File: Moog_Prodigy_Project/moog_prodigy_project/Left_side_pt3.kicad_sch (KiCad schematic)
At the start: 52 parts, among them J1 P2-3, J2 P2-4, J3 P2-2, J4 P2-1, J5 P2-1, SW6 Switch_4x4, SW7 SW_Slide_DPDT_3x3, SW9 Switch_1x3, U12B1 OPA134, U13 NE5532, U14 AD8001AR, U2 NE5532, U2B2 OPA134, U67 OPA134

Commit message: PCB priprema i fix gresaka
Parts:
- removed J1: P2-3, Connector:Banana_Cliff_FCR7350B_S16N-PC_Horizontal, symbol CT3151-2:CT3151-2
- removed J2: P2-4, Connector:Banana_Cliff_FCR7350B_S16N-PC_Horizontal, symbol CT3151-2:CT3151-2
- removed J3: P2-2, Connector:Banana_Cliff_FCR7350B_S16N-PC_Horizontal, symbol CT3151-2:CT3151-2
- removed J4, J5: P2-1, Connector:Banana_Cliff_FCR7350B_S16N-PC_Horizontal, symbol CT3151-2:CT3151-2
- removed SW9: Switch_1x3, symbol Switch:DPDT2
- removed U14: AD8001AR, Package_SO:SOIC-8_3.9x4.9mm_P1.27mm, symbol Amplifier_Operational:AD8001AR
- removed U2B2: OPA134, OPA134PA:DIP794W45P254L959H508Q8, symbol Amplifier_Operational:OPA134
- added J1: P2-3, Connector:Banana_Cliff_FCR7350B_S16N-PC_Horizontal, symbol Connector_Generic:Conn_01x01
- added J2: P2-4, Connector:Banana_Cliff_FCR7350B_S16N-PC_Horizontal, symbol Connector_Generic:Conn_01x01
- added J3: P2-2, Connector:Banana_Cliff_FCR7350B_S16N-PC_Horizontal, symbol Connector_Generic:Conn_01x01
- added J4, J5: P2-1, Connector:Banana_Cliff_FCR7350B_S16N-PC_Horizontal, symbol Connector_Generic:Conn_01x01
- added SW9: Switch_1x3, ATE1D-2M3-10-Z_1x2:SW_ATE1D-2M3-10-Z, symbol Switch:SW_SPDT
- added unit 1 of U12
- added U3: NE5532, NE5532AP:DIP794W45P254L1016H508Q8, symbol Amplifier_Operational:NE5532
- added U4: OPA134, OPA134PA:DIP794W45P254L959H508Q8, symbol Comparator:MCP6562
- added unit 1 of UI1
- added unit 3 of UI1
- R29, R79: footprint Resistor_THT:R_Axial_DIN0207_L6.3mm_D2.5mm_P7.62mm_Horizontal -> Potentiometer_THT:Potentiometer_ACP_CA9-V10_Vertical
- R92, R98: footprint Resistor_THT:R_Axial_DIN0207_L6.3mm_D2.5mm_P7.62mm_Horizontal -> Potentiometer_THT:Potentiometer_Runtron_RM-065_Vertical
- RV88: renamed from R88; footprint Resistor_THT:R_Axial_DIN0207_L6.3mm_D2.5mm_P7.62mm_Horizontal -> Potentiometer_THT:Potentiometer_ACP_CA9-V10_Vertical
- renumbered U12B1 to U12
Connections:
- net +12V: now also J5.1 (Pin_1), U3.8 (V+), U4.8 (V+), UI1.8 (V+)
- net -12V: now also U3.4 (V-), U4.4 (V-), UI1.4 (V-)
- net at C23.1, R82.2: now also U12.7; no longer U12.1
- net at C23.2, R85.2: now also U12.6 (-); no longer U12.2 (-)
- net at R81.1: now also U12.5 (+), J3.1 (Pin_1); no longer U12.3 (+)
- net at R86.2, R87.1, R89.2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: now also UI1.2 (-)
- net at C21.2, UI4.4: now also U12.3 (+)
- net at C22.2, R83.1, UI1.5 (+): now also J1.1 (Pin_1)
- net at R170.1: now also J4.1 (Pin_1)
- net at R104.1, R105.2: now also SW9.3 (C)
- net at R90.2, R91.1: now also UI1.3 (+)
- net at R85.1, R95.1, SW6.6 (F): now also U12.1, U12.2 (-)
- net at C24.1, R98.2, U13.2 (-): now also SW9.1 (A)
- net at U13.5 (+): now also SW9.2 (B)
- net at C22.1, UI1.7: now also J2.1 (Pin_1)
- net at R87.2: now also UI1.1
- no-connect marks 13 -> 11
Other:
- moved on the sheet: CR1, CR2, R105, R29, R83, R84, R86, R89, RV88, U13B, UI1B

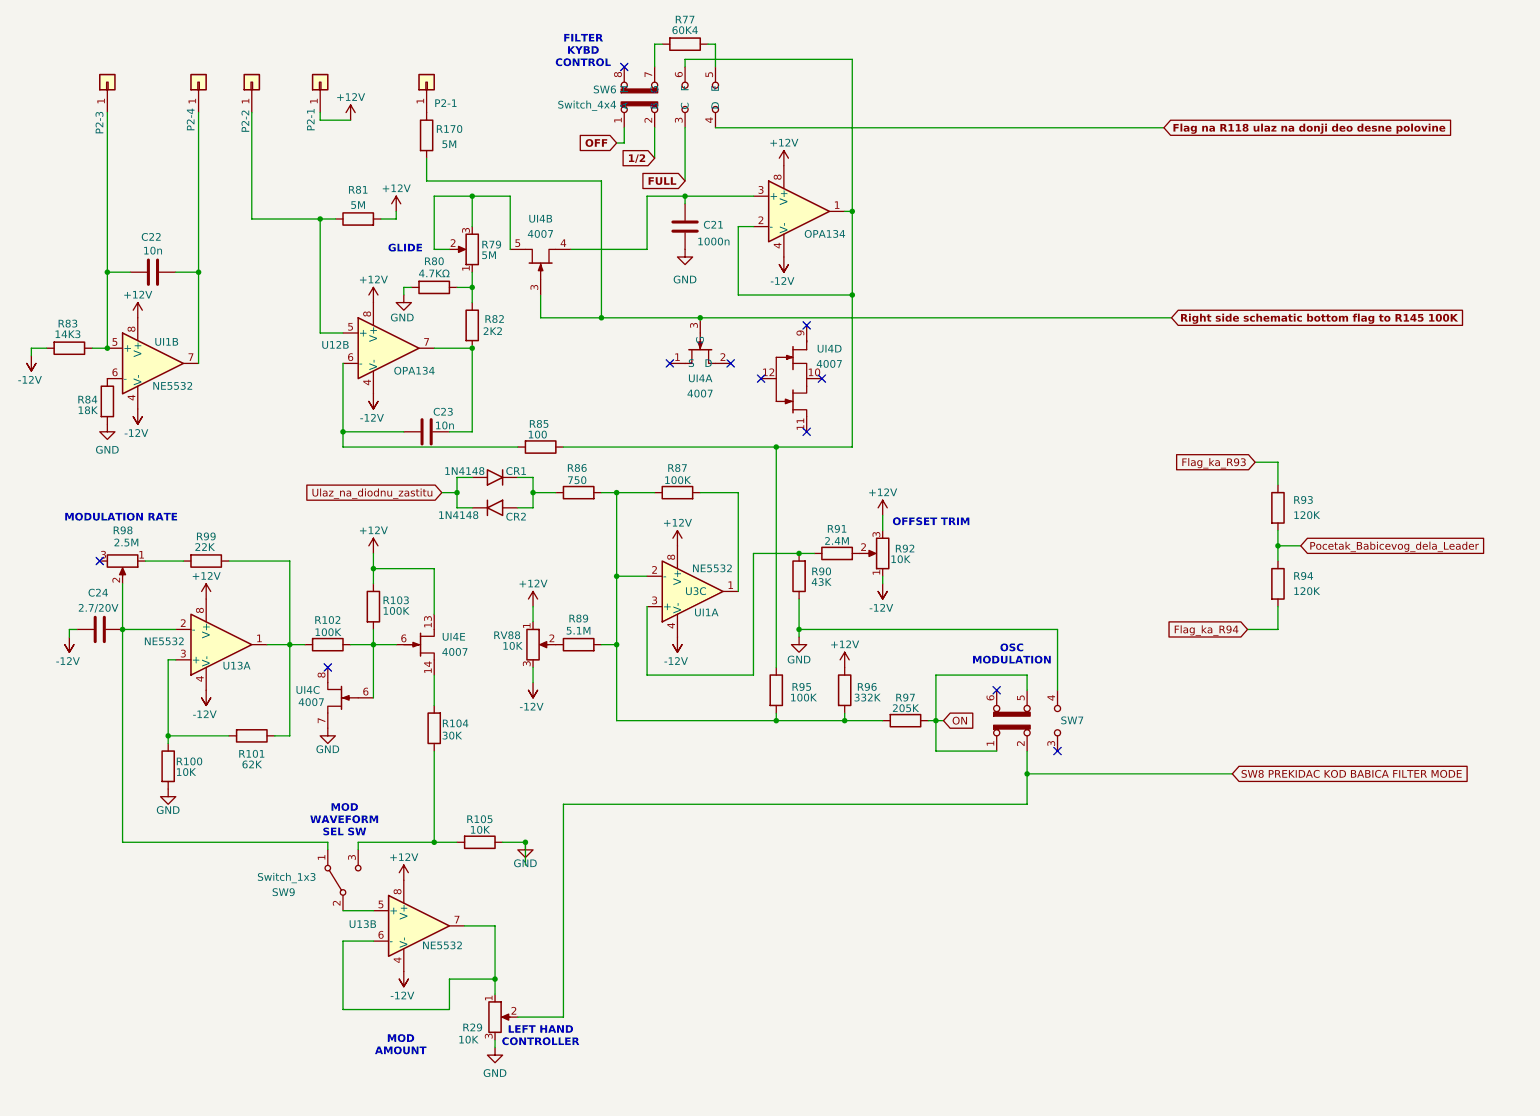
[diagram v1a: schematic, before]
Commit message: problemi sa ca3096, multiplicirani footprintovi
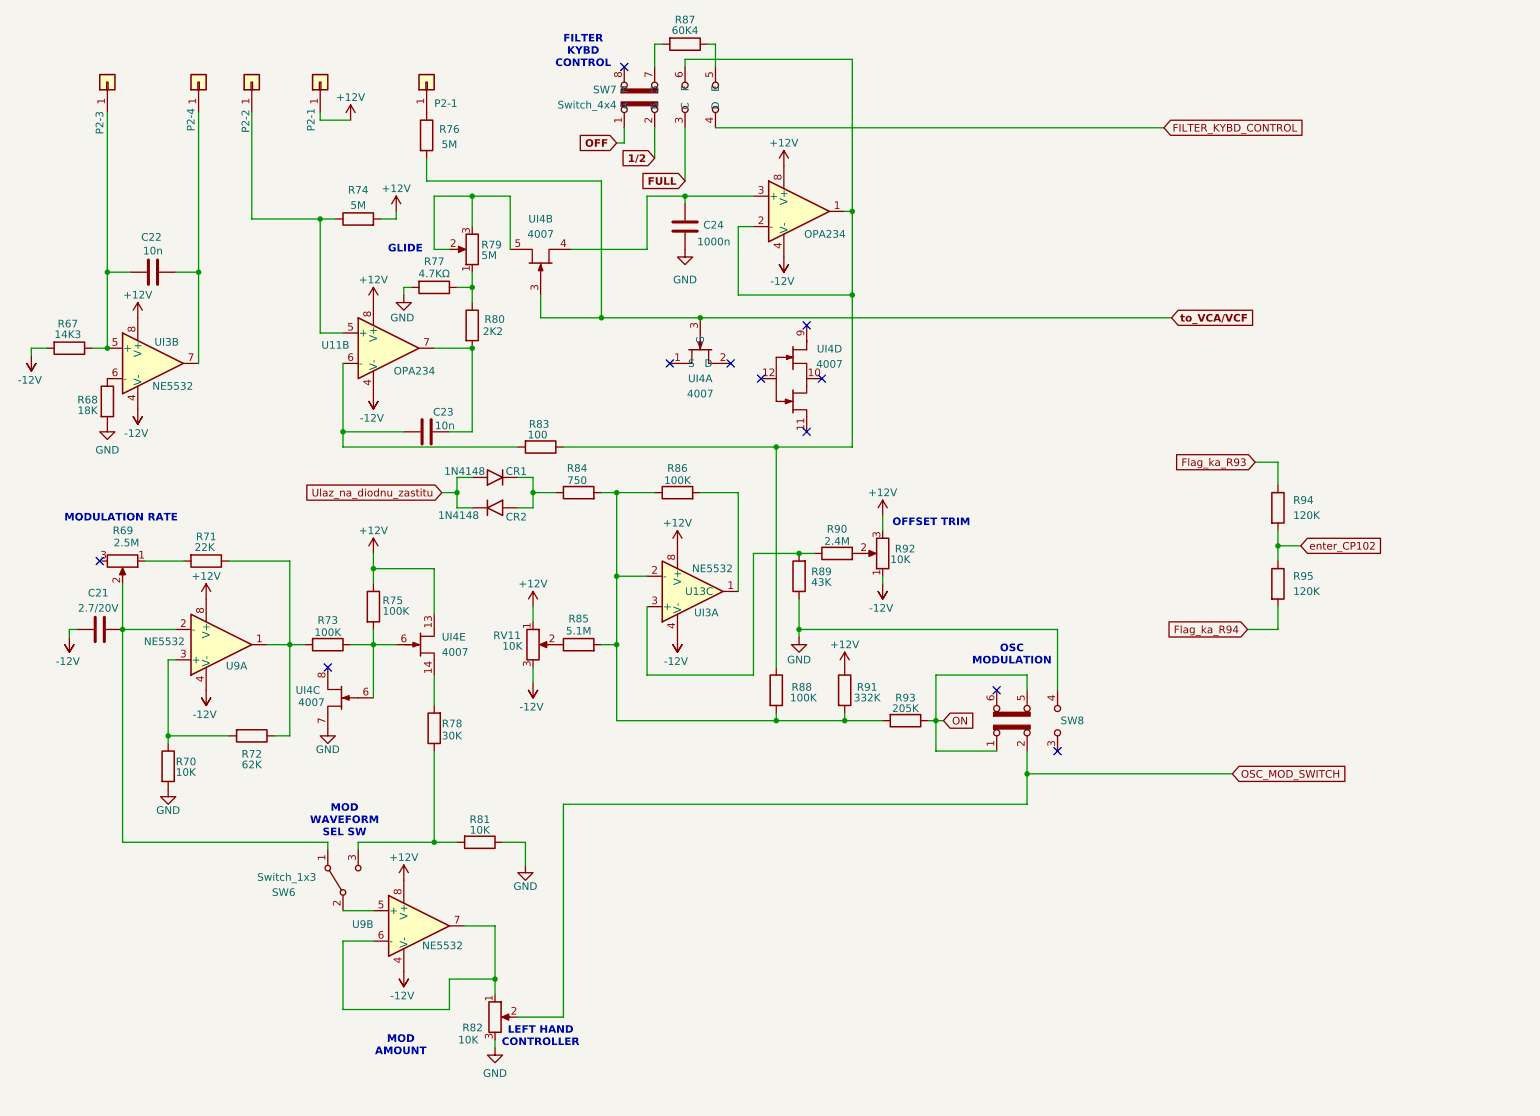
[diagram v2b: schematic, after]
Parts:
- SW8: renamed from SW7; footprint CL-SB-22A-02T_3x3:SW_CL-SB-22A-02T -> Button_Switch_THT:SW_CK_JS202011CQN_DPDT_Straight
- U11: renamed from U12; value OPA134 -> OPA234
- UI4: footprint MC14007UBDG:SOIC127P600X175-14N -> Package_DIP:DIP-14_W7.62mm_Socket
- renumbered C24 to C21, C21 to C24, J5 to J4, J4 to J5, R83 to R67, R84 to R68, R98 to R69, R100 to R70, R99 to R71, R101 to R72, R102 to R73, R81 to R74, R103 to R75, R170 to R76, R80 to R77, R104 to R78, R82 to R80, R105 to R81, R29 to R82, R85 to R83, R86 to R84, R89 to R85, R87 to R86, R77 to R87, R95 to R88, R90 to R89, R91 to R90, R96 to R91, R97 to R93, R93 to R94, R94 to R95, RV88 to RV11, SW9 to SW6, SW6 to SW7, U2 to U10, U67 to U12, U3 to U13, U4 to U14, U13 to U9, UI1 to UI3
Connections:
- net Flag na  R118 ulaz na donji deo desne polovine renamed FILTER_KYBD_CONTROL
- net Pocetak_Babicevog_dela_Leader renamed enter_CP102
- net Right side schematic bottom flag to R145 100K renamed to_VCA/VCF
- net SW8 PREKIDAC KOD BABICA FILTER MODE renamed OSC_MOD_SWITCH

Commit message: Fix 1 nakon review-a 27.05.2026
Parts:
- removed R92: 10K, Potentiometer_THT:Potentiometer_Runtron_RM-065_Vertical, symbol Device:R_Potentiometer
- added RV92: 10K, Potentiometer_THT:Potentiometer_Bourns_3339P_Vertical_HandSoldering, symbol Device:R_Potentiometer_Trim
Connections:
- net +12V: now also UI4., RV92.3; no longer UI4.13
- net -12V: now also RV92.1
- net GND: now also UI4.; no longer UI4.7
- net to_VCA/VCF: now also UI4., UI4.; no longer UI4.3, UI4.3 (G)
- net at R73.1, R75.2: now also UI4., UI4.; no longer UI4.6, UI4.6
- net at C24.2, U11.3 (+): now also UI4.; no longer UI4.4
- net at R78.2: now also UI4.; no longer UI4.14
- net at R90.2: now also RV92.2
- net at R79.2, R79.3: now also UI4.; no longer UI4.5
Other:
- title: (none) -> Treći segment leve strane šeme

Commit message: Latest checkpoints update 05.06.2026
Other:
- note added: "Oblik signala po položaju preklopnika Trouga - levi položaj Četvrtka - desni položaj"
- note added: "Paljenje OSC modulacije: ON - levi položaj preklopnika OFF - desni položaj preklopnika"
- moved on the sheet: C23, R83, SW6
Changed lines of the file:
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@@
 		(comment 4 "Jovan Mastelica E1 105/2023")
 	)
+	(text "Oblik signala po položaju preklopnika\nTrouga - levi položaj\nČetvrtka - desni položaj"
+		(exclude_from_sim no)
+		(at 48.768 147.066 0)
+		(effects
+			(font
+				(size 1.27 1.27)
+			)
+			(justify left)
+		)
+	)
 	(text "OFFSET TRIM"
 		(exclude_from_sim no)
@@
 	(text "OSC\nMODULATION"
 		(exclude_from_sim no)
-		(at 182.88 119.888 0)
+		(at 178.308 139.446 0)
 		(effects
 			(font
@@
 	(text "MOD \nWAVEFORM \nSEL SW"
 		(exclude_from_sim no)
-		(at 71.374 147.574 0)
+		(at 55.372 155.702 0)
 		(effects
 			(font
@@
 		)
 	)
+	(text "Paljenje OSC modulacije:\nON - levi položaj preklopnika\nOFF - desni položaj preklopnika"
+		(exclude_from_sim no)
+		(at 169.418 118.872 0)
+		(effects
+			(font
+				(size 1.27 1.27)
+			)
+			(justify left)
+		)
+	)
 	(text "MODULATION RATE"
 		(exclude_from_sim no)
@@
 	)
 	(junction
+		(at 71.12 82.55)
+		(diameter 0)
+		(color 0 0 0 0)
+	)
+	(junction
 		(at 90.17 92.71)
 		(diameter 0)
@@
 	)
 	(junction
-		(at 71.12 82.55)
-		(diameter 0)
-		(color 0 0 0 0)
-	)
-	(junction
 		(at 156.21 45.72)
 		(diameter 0)
@@
 	)
 	(junction
-		(at 143.51 85.09)
+		(at 143.51 86.36)
 		(diameter 0)
 		(color 0 0 0 0)
@@
 	)
 	(junction
-		(at 154.94 130.81)
+		(at 147.32 113.03)
 		(diameter 0)
 		(color 0 0 0 0)
 	)
 	(junction
-		(at 128.27 43.18)
+		(at 154.94 130.81)
 		(diameter 0)
 		(color 0 0 0 0)
 	)
 	(junction
-		(at 147.32 115.57)
+		(at 128.27 43.18)
 		(diameter 0)
 		(color 0 0 0 0)
@@
 	(wire
 		(pts
-			(xy 71.12 162.56) (xy 76.2 162.56)
+			(xy 64.77 162.56) (xy 76.2 162.56)
 		)
 		(stroke
@@
 	(wire
 		(pts
-			(xy 107.95 85.09) (xy 143.51 85.09)
+			(xy 107.95 86.36) (xy 143.51 86.36)
 		)
 		(stroke
@@
 	(wire
 		(pts
-			(xy 88.9 82.55) (xy 92.71 82.55)
+			(xy 86.36 82.55) (xy 92.71 82.55)
 		)
 		(stroke
@@
 	(wire
 		(pts
-			(xy 156.21 85.09) (xy 156.21 59.69)
+			(xy 156.21 86.36) (xy 156.21 59.69)
 		)
 		(stroke
@@
 	(wire
 		(pts
+			(xy 147.32 113.03) (xy 147.32 116.84)
+		)
+		(stroke
+			(width 0)
+			(type default)
+		)
+	)
+	(wire
+		(pts
 			(xy 76.2 105.41) (xy 76.2 107.95)
 		)
@@
 	(wire
 		(pts
-			(xy 147.32 110.49) (xy 147.32 115.57)
+			(xy 147.32 110.49) (xy 147.32 113.03)
 		)
 		(stroke
@@
 	(wire
 		(pts
-			(xy 71.12 82.55) (xy 81.28 82.55)
+			(xy 71.12 82.55) (xy 78.74 82.55)
 		)
 		(stroke
@@
 	(wire
 		(pts
-			(xy 34.29 151.13) (xy 68.58 151.13)
+			(xy 34.29 151.13) (xy 62.23 151.13)
 		)
 		(stroke
@@
 	(wire
 		(pts
+			(xy 71.12 71.12) (xy 71.12 82.55)
+		)
+		(stroke
+			(width 0)
+			(type default)
+		)
+	)
+	(wire
+		(pts
 			(xy 97.79 151.13) (xy 101.6 151.13)
 		)
@@
 	(wire
 		(pts
-			(xy 73.66 151.13) (xy 86.36 151.13)
+			(xy 67.31 151.13) (xy 86.36 151.13)
 		)
 		(stroke
@@
 	(wire
 		(pts
+			(xy 203.2 125.73) (xy 190.5 125.73)
+		)
+		(stroke
+			(width 0)
+			(type default)
+		)
+	)
+	(wire
+		(pts
 			(xy 154.94 129.54) (xy 154.94 130.81)
 		)
@@
 	(wire
 		(pts
-			(xy 71.12 85.09) (xy 100.33 85.09)
+			(xy 71.12 86.36) (xy 100.33 86.36)
 		)
 		(stroke
@@
 	(wire
 		(pts
-			(xy 143.51 85.09) (xy 143.51 121.92)
+			(xy 143.51 86.36) (xy 143.51 121.92)
 		)
 		(stroke
@@
 	(wire
 		(pts
-			(xy 156.21 85.09) (xy 143.51 85.09)
+			(xy 156.21 86.36) (xy 143.51 86.36)
 		)
 		(stroke
@@
 	(wire
 		(pts
-			(xy 147.32 115.57) (xy 190.5 115.57)
+			(xy 147.32 113.03) (xy 203.2 113.03)
 		)
 		(stroke
@@
 	(wire
 		(pts
-			(xy 190.5 115.57) (xy 190.5 125.73)
+			(xy 203.2 113.03) (xy 203.2 125.73)
 		)
 		(stroke
@@
 	(wire
 		(pts
-			(xy 71.12 71.12) (xy 71.12 82.55)
+			(xy 71.12 82.55) (xy 71.12 86.36)
 		)
 		(stroke
@@
 	(wire
 		(pts
-			(xy 71.12 82.55) (xy 71.12 85.09)
-		)
-		(stroke
-			(width 0)
-			(type default)
-		)
-	)
-	(wire
-		(pts
 			(xy 96.52 184.15) (xy 96.52 185.42)
 		)
@@
 	(wire
 		(pts
-			(xy 73.66 152.4) (xy 73.66 151.13)
+			(xy 67.31 152.4) (xy 67.31 151.13)
 		)
 		(stroke
@@
 	(wire
 		(pts
-			(xy 68.58 151.13) (xy 68.58 152.4)
+			(xy 62.23 151.13) (xy 62.23 152.4)
 		)
 		(stroke
@@
 	(wire
 		(pts
-			(xy 147.32 115.57) (xy 147.32 116.84)
-		)
-		(stroke
-			(width 0)
-			(type default)
-		)
-	)
-	(wire
-		(pts
 			(xy 96.52 165.1) (xy 96.52 173.99)
 		)
@@
 	(symbol
 		(lib_id "Device:R")
-		(at 104.14 85.09 270)
+		(at 104.14 86.36 270)
 		(unit 1)
 		(exclude_from_sim no)
@@
 		(dnp no)
 		(property "Reference" "R83"
-			(at 103.886 81.28 90)
+			(at 103.886 82.55 90)
 			(effects
 				(font
@@
 		)
 		(property "Value" "100"
-			(at 103.632 83.058 90)
+			(at 103.632 84.328 90)
 			(effects
 				(font
@@
 		)
 		(property "Footprint" "Resistor_THT:R_Axial_DIN0207_L6.3mm_D2.5mm_P7.62mm_Horizontal"
-			(at 104.14 83.312 90)
+			(at 104.14 84.582 90)
 			(effects
 				(font
@@
 		)
 		(property "Datasheet" "~"
-			(at 104.14 85.09 0)
+			(at 104.14 86.36 0)
 			(effects
 				(font
@@
 		)
 		(property "Description" "Resistor"
-			(at 104.14 85.09 0)
+			(at 104.14 86.36 0)
 			(effects
 				(font
@@
 		(lib_name "SW_SPDT_1")
 		(lib_id "Switch:SW_SPDT")
-		(at 71.12 157.48 90)
+		(at 64.77 157.48 90)
 		(unit 1)
 		(exclude_from_sim no)
@@
 		(dnp no)
 		(property "Reference" "SW6"
-			(at 61.214 159.512 90)
+			(at 68.072 158.496 90)
 			(effects
 				(font
@@
 		)
 		(property "Value" "Switch_1x3"
-			(at 61.722 156.972 90)
+			(at 55.372 156.972 90)
 			(effects
 				(font
 					(size 1.27 1.27)
 				)
+				(hide yes)
 			)
 		)
 		(property "Footprint" "ATE1D-2M3-10-Z_1x2:SW_ATE1D-2M3-10-Z"
-			(at 71.12 157.48 0)
+			(at 64.77 157.48 0)
 			(effects
 				(font
@@
 		)
 		(property "Datasheet" "~"
-			(at 78.74 157.48 0)
+			(at 72.39 157.48 0)
 			(effects
 				(font
@@
 		)
 		(property "Description" "Switch, single pole double throw"
-			(at 71.12 157.48 0)
+			(at 64.77 157.48 0)
 			(effects
 				(font
@@
 	(symbol
 		(lib_id "Device:C")
-		(at 85.09 82.55 270)
+		(at 82.55 82.55 270)
 		(unit 1)
 		(exclude_from_sim no)
@@
 		(dnp no)
 		(property "Reference" "C23"
-			(at 87.884 79.248 90)
+			(at 85.344 79.248 90)
 			(effects
 				(font
@@
 		)
 		(property "Value" "10n"
-			(at 88.138 81.534 90)
+			(at 85.598 81.534 90)
 			(effects
 				(font
@@
 		)
 		(property "Footprint" "Capacitor_THT:C_Disc_D3.8mm_W2.6mm_P2.50mm"
-			(at 81.28 83.5152 0)
+			(at 78.74 83.5152 0)
 			(effects
 				(font
@@
 		)
 		(property "Datasheet" "~"
-			(at 85.09 82.55 0)
+			(at 82.55 82.55 0)
 			(effects
 				(font
@@
 		)
 		(property "Description" "Unpolarized capacitor"
-			(at 85.09 82.55 0)
+			(at 82.55 82.55 0)
 			(effects
 				(font
@@
 		(fields_autoplaced yes)
 		(property "Reference" "SW7"
-			(at 116.84 25.3999 0)
+			(at 116.84 26.6699 0)
 			(effects
 				(font
@@
 				)
 				(justify right)
+				(hide yes)
 			)
 		)

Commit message: 27.06.2026 - dodavanje izmena sa konsultacija
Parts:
- added C59, C60, C61, C62, C63, C64, C65, C66, C67, C68, C69, C70: 100n, Capacitor_THT:CP_Radial_D5.0mm_P2.50mm, symbol Device:C
- renumbered UI4 to 1_UI4, UI4 to 2_UI4, UI4 to 3_UI4, UI4 to 4_UI4, UI4 to 5_UI4
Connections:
- net +12V: now also C60.2, C62.2, C63.2, C65.2, C68.2, C70.2
- net -12V: now also C59.2, C61.2, C64.2, C66.2, C67.2, C69.2
- net GND: now also C59.1, C60.1, C61.1, C62.1, C63.1, C64.1, C65.1, C66.1, C67.1, C68.1, C69.1, C70.1
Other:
- note added: "NAPOMENA Kondenzatori: C59,C60,C61,C62,C63,C64, C65,C66,C67,C68,C69,C70 su vrednosti 100n i oni su kvalitetniji"
- note added: "ON OFF"
- note added: "Oblik signala po položaju preklopnika Trougao Četvrtka"
- note removed: "Oblik signala po položaju preklopnika Trouga - levi položaj Četvrtka - desni položaj"
- note removed: "Paljenje OSC modulacije: ON - levi položaj preklopnika OFF - desni položaj preklopnika"
- moved on the sheet: 3_UI4C, C22, C23, R73, R75, R82
